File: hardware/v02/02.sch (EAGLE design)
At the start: 33 parts, among them IC1 MSP430G2553, IC2 78L05Z, X2 RJ45-6L-B

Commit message: rearrange
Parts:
- removed R11, R12, R13, R14: 10k, rcl:R-EU_0207/10
- removed R5, R6, R7, R8: 220, rcl:R-EU_0207/10
- added RN1: 4.7k, resistor-net:RN04
- added RN2: 220, resistor-net:RN04
- R1, R10, R2, R3, R4: device rcl:R-EU_0207/10 -> rcl:R-EU_0207/12
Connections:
- removed net N$17: LED2.C, R6.2
- removed net N$21: LED3.C, R7.2
- new net N$10: LED2.A, RN2.3
- new net N$14: LED4.A, RN2.5
- net +5V: now also RN1.1, X2.3; no longer JP5.4, R11.2, R12.2, R13.2, R14.2, X2.2
- net GND: now also X2.5; no longer X2.3
- net N$12: now also LED1.C; no longer R5.1
- net N$13: now also LED3.A, RN2.4; no longer LED1.C, R5.2
- net N$8: now also LED1.A, RN2.2; no longer LED4.C, R8.2
- net N$9: now also LED2.C; no longer R6.1
- net OUT1: now also RN1.2, X2.2; no longer R11.1, X2.4
- net OUT2: now also RN1.3, X2.4; no longer R12.1, X2.5
- net OUT3: now also RN1.4; no longer R13.1
- net OUT4: now also RN1.5; no longer R14.1
- net PB: now also LED4.C; no longer R8.1
- net PR: now also LED3.C; no longer R7.1
- net VCC: now also JP5.4, RN2.1; no longer LED1.A, LED2.A, LED3.A, LED4.A
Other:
- moved on the sheet: LED1, LED2, LED3, LED4

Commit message: smaller IC; rearrange
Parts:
- removed IC1: MSP430G2553, ic-package:DIL20
- added IC3: MSP430G2553, ic-package:DIL14S
- R10: device rcl:R-EU_0207/12 -> rcl:R-EU_0207/7
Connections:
- net GND: now also IC3.14; no longer IC1.20
- net N$1: now also IC3.6; no longer IC1.6
- net N$12: now also IC3.2; no longer IC1.2
- net N$2: now also IC3.13; no longer IC1.19
- net N$3: now also IC3.7; no longer IC1.7
- net N$4: now also IC3.8; no longer IC1.14
- net N$5: now also IC3.10; no longer IC1.16
- net N$6: now also IC3.11; no longer IC1.17
- net N$7: now also IC3.12; no longer IC1.18
- net N$9: now also IC3.3; no longer IC1.3
- net PB: now also IC3.5; no longer IC1.5
- net PR: now also IC3.4; no longer IC1.4
- net VCC: now also IC3.1; no longer IC1.1
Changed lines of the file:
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@@
 <part name="GND1" library="supply1" deviceset="GND" device=""/>
 <part name="P+2" library="supply1" deviceset="+5V" device=""/>
-<part name="IC1" library="ic-package" deviceset="DIL20" device="" value="MSP430G2553"/>
 <part name="C1" library="rcl" deviceset="C-EU" device="025-024X044" value="100nF"/>
 <part name="C2" library="rcl" deviceset="C-EU" device="025-024X044" value="100nF"/>
@@
 <part name="P+8" library="supply1" deviceset="+5V" device=""/>
 <part name="GND4" library="supply1" deviceset="GND" device=""/>
-<part name="R10" library="rcl" deviceset="R-EU_" device="0207/12" value="47k"/>
+<part name="R10" library="rcl" deviceset="R-EU_" device="0207/7" value="47k"/>
 <part name="C3" library="rcl" deviceset="C-EU" device="025-024X044" value="100nF"/>
 <part name="C4" library="rcl" deviceset="CPOL-EU" device="B45181A" value="200nF"/>
@@
 <part name="RN2" library="resistor-net" deviceset="RN04" device="" value="220"/>
 <part name="P+4" library="supply1" deviceset="VCC" device=""/>
+<part name="IC3" library="ic-package" deviceset="DIL14" device="S" value="MSP430G2553"/>
 </parts>
 <sheets>
@@
 <instance part="GND1" gate="1" x="106.68" y="27.94"/>
 <instance part="P+2" gate="1" x="144.78" y="121.92"/>
-<instance part="IC1" gate="G$1" x="129.54" y="58.42"/>
 <instance part="C1" gate="G$1" x="114.3" y="38.1" rot="MR0"/>
 <instance part="C2" gate="G$1" x="144.78" y="38.1"/>
@@
 <instance part="RN2" gate="1" x="83.82" y="93.98"/>
 <instance part="P+4" gate="VCC" x="167.64" y="68.58"/>
+<instance part="IC3" gate="G$1" x="129.54" y="60.96"/>
 </instances>
 <busses>
@@
 <wire x1="106.68" y1="68.58" x2="114.3" y2="68.58" width="0.1524" layer="91"/>
 <pinref part="P+1" gate="VCC" pin="VCC"/>
-<pinref part="IC1" gate="G$1" pin="1"/>
 <pinref part="R10" gate="G$1" pin="1"/>
 <wire x1="154.94" y1="48.26" x2="154.94" y2="43.18" width="0.1524" layer="91"/>
@@
 <junction x="106.68" y="43.18"/>
 <wire x1="106.68" y1="43.18" x2="106.68" y2="68.58" width="0.1524" layer="91"/>
+<pinref part="IC3" gate="G$1" pin="1"/>
 </segment>
 <segment>
@@
 <label x="109.22" y="60.96" size="1.778" layer="95"/>
 <pinref part="R3" gate="G$1" pin="1"/>
-<pinref part="IC1" gate="G$1" pin="4"/>
 <wire x1="99.06" y1="73.66" x2="99.06" y2="60.96" width="0.1524" layer="91"/>
 <junction x="99.06" y="60.96"/>
 <pinref part="LED3" gate="G$1" pin="C"/>
+<pinref part="IC3" gate="G$1" pin="4"/>
 </segment>
 </net>
@@
 <label x="109.22" y="58.42" size="1.778" layer="95"/>
 <pinref part="R4" gate="G$1" pin="1"/>
-<pinref part="IC1" gate="G$1" pin="5"/>
 <wire x1="104.14" y1="58.42" x2="121.92" y2="58.42" width="0.1524" layer="91"/>
 <wire x1="104.14" y1="68.58" x2="104.14" y2="58.42" width="0.1524" layer="91"/>
 <junction x="104.14" y="58.42"/>
 <pinref part="LED4" gate="G$1" pin="C"/>
+<pinref part="IC3" gate="G$1" pin="5"/>
 </segment>
 </net>
@@
 <wire x1="111.76" y1="55.88" x2="111.76" y2="40.64" width="0.1524" layer="91"/>
 <wire x1="111.76" y1="40.64" x2="106.68" y2="40.64" width="0.1524" layer="91"/>
-<pinref part="IC1" gate="G$1" pin="6"/>
 <pinref part="JP3" gate="A" pin="2"/>
+<pinref part="IC3" gate="G$1" pin="6"/>
 </segment>
 </net>
@@
 <pinref part="C1" gate="G$1" pin="2"/>
 <pinref part="C2" gate="G$1" pin="2"/>
-<pinref part="IC1" gate="G$1" pin="20"/>
 <pinref part="JP3" gate="A" pin="1"/>
 <pinref part="JP4" gate="A" pin="2"/>
@@
 <wire x1="149.86" y1="50.8" x2="149.86" y2="30.48" width="0.1524" layer="91"/>
 <junction x="149.86" y="30.48"/>
+<pinref part="IC3" gate="G$1" pin="14"/>
 </segment>
 <segment>
@@
 <wire x1="127" y1="40.64" x2="127" y2="35.56" width="0.1524" layer="91"/>
 <junction x="114.3" y="40.64"/>
-<pinref part="IC1" gate="G$1" pin="7"/>
 <pinref part="C1" gate="G$1" pin="1"/>
 <pinref part="JP4" gate="A" pin="3"/>
+<pinref part="IC3" gate="G$1" pin="7"/>
 </segment>
 </net>
@@
 <wire x1="132.08" y1="40.64" x2="132.08" y2="35.56" width="0.1524" layer="91"/>
 <junction x="144.78" y="40.64"/>
-<pinref part="IC1" gate="G$1" pin="14"/>
 <pinref part="C2" gate="G$1" pin="1"/>
 <pinref part="JP4" gate="A" pin="1"/>
+<pinref part="IC3" gate="G$1" pin="8"/>
 </segment>
 </net>
@@
 <segment>
 <wire x1="172.72" y1="58.42" x2="154.94" y2="58.42" width="0.1524" layer="91"/>
-<pinref part="IC1" gate="G$1" pin="16"/>
 <pinref part="JP5" gate="A" pin="2"/>
 <pinref part="R10" gate="G$1" pin="2"/>
@@
 <wire x1="149.86" y1="58.42" x2="137.16" y2="58.42" width="0.1524" layer="91"/>
 <junction x="149.86" y="58.42"/>
+<pinref part="IC3" gate="G$1" pin="10"/>
 </segment>
 </net>
@@
 <segment>
 <wire x1="137.16" y1="60.96" x2="172.72" y2="60.96" width="0.1524" layer="91"/>
-<pinref part="IC1" gate="G$1" pin="17"/>
 <pinref part="JP5" gate="A" pin="1"/>
 <label x="142.24" y="60.96" size="1.778" layer="95"/>
+<pinref part="IC3" gate="G$1" pin="11"/>
 </segment>
 </net>
@@
 <wire x1="139.7" y1="66.04" x2="137.16" y2="66.04" width="0.1524" layer="91"/>
 <pinref part="XTAL" gate="G$1" pin="1"/>
-<pinref part="IC1" gate="G$1" pin="19"/>
+<pinref part="IC3" gate="G$1" pin="13"/>
 </segment>
 </net>
@@
 <wire x1="147.32" y1="63.5" x2="137.16" y2="63.5" width="0.1524" layer="91"/>
 <pinref part="XTAL" gate="G$1" pin="2"/>
-<pinref part="IC1" gate="G$1" pin="18"/>
+<pinref part="IC3" gate="G$1" pin="12"/>
 </segment>
 </net>
@@
 <wire x1="121.92" y1="63.5" x2="93.98" y2="63.5" width="0.1524" layer="91"/>
 <pinref part="R2" gate="G$1" pin="1"/>
-<pinref part="IC1" gate="G$1" pin="3"/>
 <wire x1="93.98" y1="63.5" x2="86.36" y2="63.5" width="0.1524" layer="91"/>
 <wire x1="86.36" y1="63.5" x2="86.36" y2="58.42" width="0.1524" layer="91"/>
@@
 <junction x="93.98" y="63.5"/>
 <pinref part="LED2" gate="G$1" pin="C"/>
+<pinref part="IC3" gate="G$1" pin="3"/>
 </segment>
 </net>
@@
 <wire x1="121.92" y1="66.04" x2="88.9" y2="66.04" width="0.1524" layer="91"/>
 <wire x1="88.9" y1="66.04" x2="58.42" y2="66.04" width="0.1524" layer="91"/>
-<pinref part="IC1" gate="G$1" pin="2"/>
 <pinref part="R1" gate="G$1" pin="1"/>
 <wire x1="88.9" y1="83.82" x2="88.9" y2="66.04" width="0.1524" layer="91"/>
 <junction x="88.9" y="66.04"/>
 <pinref part="LED1" gate="G$1" pin="C"/>
-</segment>
-</net>
+<pinref part="IC3" gate="G$1" pin="2"/>
+</segment>
+</net>

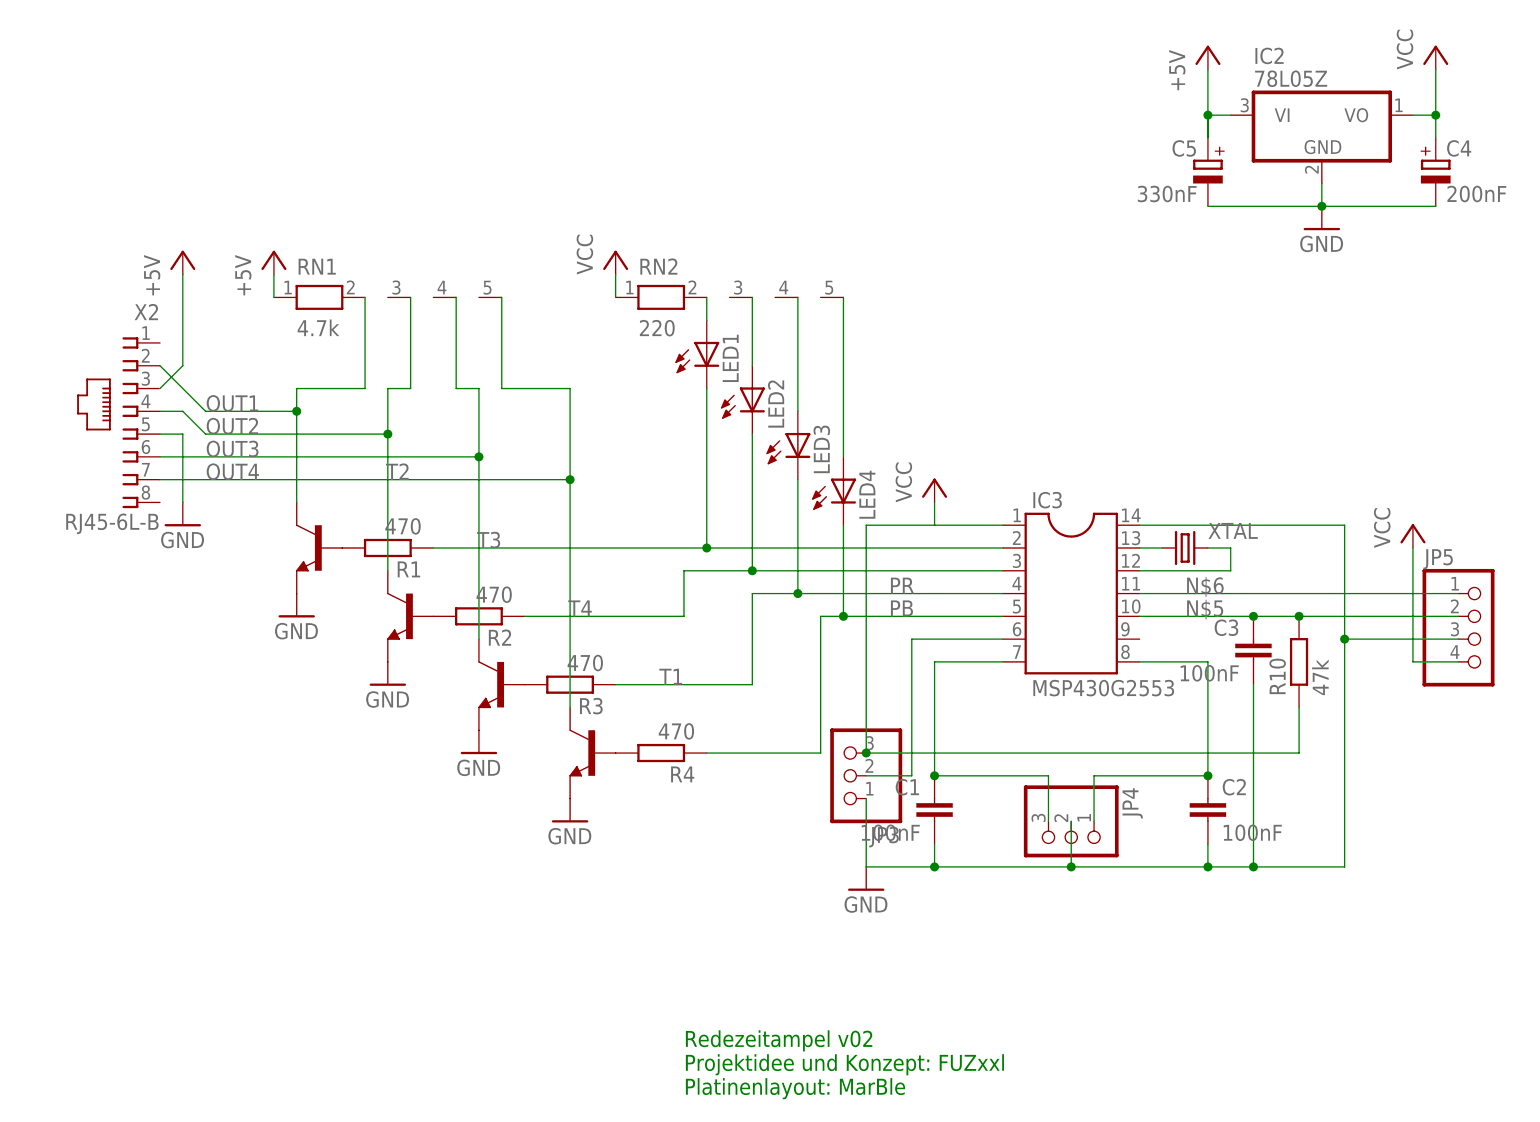
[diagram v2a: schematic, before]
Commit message: all caps converted to ceramic; diode over Vreg
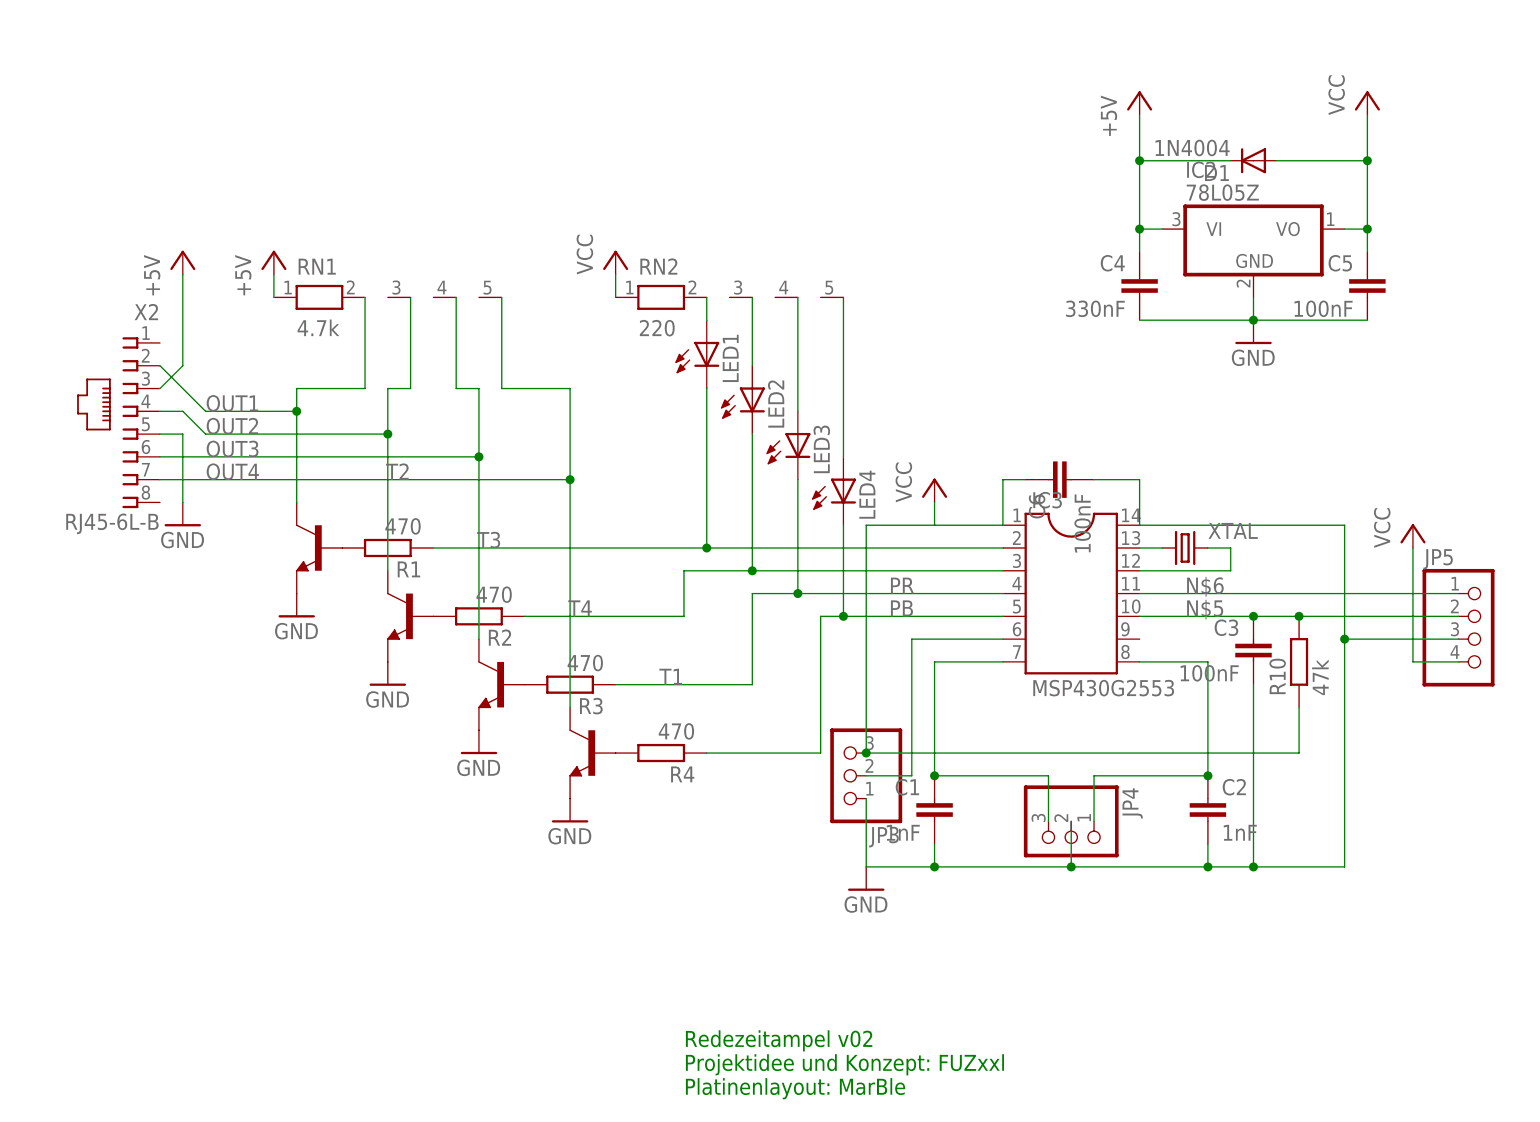
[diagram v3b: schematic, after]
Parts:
- added C6: 100nF, rcl:C-EU050-024X044
- added D1: 1N4004, adafruit:1N4004
- C1, C2: value 100nF -> 1nF
- C4: value 200nF -> 330nF; device rcl:CPOL-EUB45181A -> rcl:C-EU050-024X044
- C5: value 330nF -> 100nF; device rcl:CPOL-EUB45181A -> rcl:C-EU050-024X044
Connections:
- net +5V: now also C4.1, D1.C; no longer C5.+
- net GND: now also C4.2, C5.2, C6.2; no longer C4.-, C5.-
- net VCC: now also C5.1, C6.1, D1.A; no longer C4.+
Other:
- moved on the sheet: IC2
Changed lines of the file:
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@@
 <part name="GND1" library="supply1" deviceset="GND" device=""/>
 <part name="P+2" library="supply1" deviceset="+5V" device=""/>
-<part name="C1" library="rcl" deviceset="C-EU" device="025-024X044" value="100nF"/>
-<part name="C2" library="rcl" deviceset="C-EU" device="025-024X044" value="100nF"/>
+<part name="C1" library="rcl" deviceset="C-EU" device="025-024X044" value="1nF"/>
+<part name="C2" library="rcl" deviceset="C-EU" device="025-024X044" value="1nF"/>
 <part name="XTAL" library="crystal" deviceset="CRYSTAL" device="TC26H"/>
 <part name="R4" library="rcl" deviceset="R-EU_" device="0207/12" value="470"/>
@@
 <part name="P+7" library="supply1" deviceset="VCC" device=""/>
 <part name="GND6" library="supply1" deviceset="GND" device=""/>
-<part name="C5" library="rcl" deviceset="CPOL-EU" device="B45181A" value="330nF"/>
 <part name="T1" library="transistor" deviceset="*-NPN-" device="TO92-EBC"/>
 <part name="R1" library="rcl" deviceset="R-EU_" device="0207/12" value="470"/>
@@
 <part name="R10" library="rcl" deviceset="R-EU_" device="0207/7" value="47k"/>
 <part name="C3" library="rcl" deviceset="C-EU" device="025-024X044" value="100nF"/>
-<part name="C4" library="rcl" deviceset="CPOL-EU" device="B45181A" value="200nF"/>
 <part name="P+10" library="supply1" deviceset="VCC" device=""/>
 <part name="FRAME1" library="frames" deviceset="DINA5_L" device=""/>
@@
 <part name="P+4" library="supply1" deviceset="VCC" device=""/>
 <part name="IC3" library="ic-package" deviceset="DIL14" device="S" value="MSP430G2553"/>
+<part name="C4" library="rcl" deviceset="C-EU" device="050-024X044" value="330nF"/>
+<part name="C5" library="rcl" deviceset="C-EU" device="050-024X044" value="100nF"/>
+<part name="C6" library="rcl" deviceset="C-EU" device="050-024X044" value="100nF"/>
+<part name="D1" library="adafruit" deviceset="1N4004" device=""/>
 </parts>
 <sheets>
@@
 <instance part="P+1" gate="VCC" x="114.3" y="73.66"/>
 <instance part="GND1" gate="1" x="106.68" y="27.94"/>
-<instance part="P+2" gate="1" x="144.78" y="121.92"/>
+<instance part="P+2" gate="1" x="137.16" y="116.84"/>
 <instance part="C1" gate="G$1" x="114.3" y="38.1" rot="MR0"/>
 <instance part="C2" gate="G$1" x="144.78" y="38.1"/>
@@
 <instance part="LED4" gate="G$1" x="104.14" y="73.66"/>
 <instance part="GND5" gate="1" x="73.66" y="35.56"/>
-<instance part="IC2" gate="A1" x="157.48" y="114.3"/>
-<instance part="P+7" gate="VCC" x="170.18" y="121.92"/>
-<instance part="GND6" gate="1" x="157.48" y="101.6"/>
-<instance part="C5" gate="G$1" x="144.78" y="109.22" rot="MR0"/>
+<instance part="IC2" gate="A1" x="149.86" y="101.6"/>
+<instance part="P+7" gate="VCC" x="162.56" y="116.84"/>
+<instance part="GND6" gate="1" x="149.86" y="88.9"/>
 <instance part="T1" gate="G$1" x="76.2" y="43.18" rot="MR0"/>
 <instance part="R1" gate="G$1" x="53.34" y="66.04" rot="R180"/>
@@
 <instance part="R10" gate="G$1" x="154.94" y="53.34" rot="R90"/>
 <instance part="C3" gate="G$1" x="149.86" y="55.88" rot="MR0"/>
-<instance part="C4" gate="G$1" x="170.18" y="109.22"/>
 <instance part="P+10" gate="VCC" x="78.74" y="99.06"/>
 <instance part="FRAME1" gate="G$1" x="0" y="0"/>
@@
 <instance part="P+4" gate="VCC" x="167.64" y="68.58"/>
 <instance part="IC3" gate="G$1" x="129.54" y="60.96"/>
+<instance part="C4" gate="G$1" x="137.16" y="96.52" rot="MR0"/>
+<instance part="C5" gate="G$1" x="162.56" y="96.52" rot="MR0"/>
+<instance part="C6" gate="G$1" x="127" y="73.66" rot="MR270"/>
+<instance part="D1" gate="1" x="149.86" y="109.22" rot="R180"/>
 </instances>
 <busses>
@@
 <wire x1="106.68" y1="43.18" x2="106.68" y2="68.58" width="0.1524" layer="91"/>
 <pinref part="IC3" gate="G$1" pin="1"/>
-</segment>
-<segment>
-<wire x1="170.18" y1="114.3" x2="170.18" y2="119.38" width="0.1524" layer="91"/>
-<wire x1="170.18" y1="111.76" x2="170.18" y2="114.3" width="0.1524" layer="91"/>
-<wire x1="170.18" y1="114.3" x2="167.64" y2="114.3" width="0.1524" layer="91"/>
-<junction x="170.18" y="114.3"/>
+<wire x1="124.46" y1="73.66" x2="121.92" y2="73.66" width="0.1524" layer="91"/>
+<wire x1="121.92" y1="73.66" x2="121.92" y2="68.58" width="0.1524" layer="91"/>
+<pinref part="C6" gate="G$1" pin="1"/>
+</segment>
+<segment>
+<wire x1="162.56" y1="101.6" x2="162.56" y2="109.22" width="0.1524" layer="91"/>
+<wire x1="162.56" y1="109.22" x2="162.56" y2="114.3" width="0.1524" layer="91"/>
+<wire x1="162.56" y1="99.06" x2="162.56" y2="101.6" width="0.1524" layer="91"/>
+<wire x1="162.56" y1="101.6" x2="160.02" y2="101.6" width="0.1524" layer="91"/>
+<junction x="162.56" y="101.6"/>
 <pinref part="IC2" gate="A1" pin="VO"/>
 <pinref part="P+7" gate="VCC" pin="VCC"/>
-<pinref part="C4" gate="G$1" pin="+"/>
+<pinref part="C5" gate="G$1" pin="1"/>
+<pinref part="D1" gate="1" pin="A"/>
+<wire x1="152.4" y1="109.22" x2="162.56" y2="109.22" width="0.1524" layer="91"/>
+<junction x="162.56" y="109.22"/>
 </segment>
 <segment>
@@
 <junction x="149.86" y="30.48"/>
 <pinref part="IC3" gate="G$1" pin="14"/>
-</segment>
-<segment>
-<wire x1="157.48" y1="106.68" x2="157.48" y2="104.14" width="0.1524" layer="91"/>
-<wire x1="144.78" y1="104.14" x2="157.48" y2="104.14" width="0.1524" layer="91"/>
-<wire x1="170.18" y1="104.14" x2="157.48" y2="104.14" width="0.1524" layer="91"/>
-<junction x="157.48" y="104.14"/>
+<wire x1="132.08" y1="73.66" x2="137.16" y2="73.66" width="0.1524" layer="91"/>
+<wire x1="137.16" y1="73.66" x2="137.16" y2="68.58" width="0.1524" layer="91"/>
+<pinref part="C6" gate="G$1" pin="2"/>
+</segment>
+<segment>
+<wire x1="149.86" y1="93.98" x2="149.86" y2="91.44" width="0.1524" layer="91"/>
+<wire x1="137.16" y1="91.44" x2="149.86" y2="91.44" width="0.1524" layer="91"/>
+<wire x1="162.56" y1="91.44" x2="149.86" y2="91.44" width="0.1524" layer="91"/>
+<junction x="149.86" y="91.44"/>
 <pinref part="IC2" gate="A1" pin="GND"/>
 <pinref part="GND6" gate="1" pin="GND"/>
-<pinref part="C5" gate="G$1" pin="-"/>
-<pinref part="C4" gate="G$1" pin="-"/>
+<pinref part="C4" gate="G$1" pin="2"/>
+<pinref part="C5" gate="G$1" pin="2"/>
 </segment>
 <segment>
@@
 <net name="+5V" class="0">
 <segment>
-<wire x1="144.78" y1="119.38" x2="144.78" y2="111.76" width="0.1524" layer="91"/>
-<wire x1="144.78" y1="111.76" x2="144.78" y2="114.3" width="0.1524" layer="91"/>
-<wire x1="144.78" y1="114.3" x2="147.32" y2="114.3" width="0.1524" layer="91"/>
-<junction x="144.78" y="114.3"/>
+<wire x1="137.16" y1="114.3" x2="137.16" y2="109.22" width="0.1524" layer="91"/>
+<wire x1="137.16" y1="109.22" x2="137.16" y2="101.6" width="0.1524" layer="91"/>
+<wire x1="137.16" y1="99.06" x2="137.16" y2="101.6" width="0.1524" layer="91"/>
+<wire x1="137.16" y1="101.6" x2="139.7" y2="101.6" width="0.1524" layer="91"/>
+<junction x="137.16" y="101.6"/>
 <pinref part="P+2" gate="1" pin="+5V"/>
 <pinref part="IC2" gate="A1" pin="VI"/>
-<pinref part="C5" gate="G$1" pin="+"/>
-</segment>
-<segment>
+<pinref part="C4" gate="G$1" pin="1"/>
+<pinref part="D1" gate="1" pin="C"/>
+<wire x1="147.32" y1="109.22" x2="137.16" y2="109.22" width="0.1524" layer="91"/>
+<junction x="137.16" y="109.22"/>
+</segment>
+<segment>
